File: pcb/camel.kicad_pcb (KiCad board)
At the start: 2 copper layers, 75 x 14 mm, 49 parts, among them J1 Conn_01x04, J2 Conn_01x04, Q1 MMBT4403, Q2 MMBT4403, U1 HX711, U2 HX711, U3 MCP1700T-3302E/TT, Y1 11.0592MHz, Y2 11.0592MHz

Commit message: first pass
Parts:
- removed the C13 at (159.3, 103.2)
- removed FPC1: FPC-05F-12PH15, EasyEDA2KiCAD:FPC-SMD_12P-P0.50_XUNPU_FPC-05F-12PH15
- removed JP1, JP4, JP6: SolderJumper_2_Bridged, Jumper:SolderJumper-2_P1.3mm_Bridged_RoundedPad1.0x1.5mm
- removed JP2, JP3: SolderJumper_3_Bridged12, Jumper:SolderJumper-3_P1.3mm_Bridged12_RoundedPad1.0x1.5mm
- removed JP5, JP7: SolderJumper_2_Open, Jumper:SolderJumper-2_P1.3mm_Open_RoundedPad1.0x1.5mm
- removed the R10 at (159.3, 101.8)
- removed the R9 at (138.2, 108.2)
- removed Y1, Y2: 11.0592MHz, Crystal:Crystal_SMD_5032-4Pin_5.0x3.2mm
- added C15: 100n, Capacitor_SMD:C_0402_1005Metric, F.Cu at (143.5, 103.8)
- added C3: 10n, Capacitor_SMD:C_0402_1005Metric, F.Cu at (157.3, 112.4)
- added C4: 1u, Capacitor_SMD:C_0402_1005Metric, F.Cu at (157.3, 113.5)
- added C7: 100n, Capacitor_SMD:C_0402_1005Metric, F.Cu at (138.4, 101.5)
- added C8: 100n, Capacitor_SMD:C_0402_1005Metric, F.Cu at (153.0, 105.1)
- added D1: RED, LED_SMD:LED_0603_1608Metric, F.Cu at (140.2, 94.7)
- added D10: RCLAMP0521P-N, camel:X1-DFN1006-2_L1.0-W0.6-BI, F.Cu at (144.3, 109.9)
- added D11: RCLAMP0521P-N, camel:X1-DFN1006-2_L1.0-W0.6-BI, F.Cu at (148.0, 109.9)
- added D2: RCLAMP0521P-N, camel:X1-DFN1006-2_L1.0-W0.6-BI, F.Cu at (154.9, 97.0)
- added D3: RCLAMP0521P-N, camel:X1-DFN1006-2_L1.0-W0.6-BI, F.Cu at (160.3, 91.9)
- added D4: RCLAMP0521P-N, camel:X1-DFN1006-2_L1.0-W0.6-BI, F.Cu at (163.1, 91.9)
- added D5: RCLAMP0521P-N, camel:X1-DFN1006-2_L1.0-W0.6-BI, F.Cu at (162.9, 98.2)
- added D6: RCLAMP0521P-N, camel:X1-DFN1006-2_L1.0-W0.6-BI, F.Cu at (160.1, 98.2)
- added D7: RCLAMP0521P-N, camel:X1-DFN1006-2_L1.0-W0.6-BI, F.Cu at (148.5, 100.3)
- added D8: RCLAMP0521P-N, camel:X1-DFN1006-2_L1.0-W0.6-BI, F.Cu at (145.7, 100.3)
- added D9: RCLAMP0521P-N, camel:X1-DFN1006-2_L1.0-W0.6-BI, F.Cu at (150.9, 109.9)
- added G***: LOGO, camel:camel_logo_10, F.Cu at (164.3, 115.7)
- added G***: LOGO, camel:camel_logo_10, B.Cu at (147.1, 102.7)
- added H3: MountingHole, MountingHole:MountingHole_3.5mm, F.Cu at (174.0, 95.0)
- added H4: MountingHole, MountingHole:MountingHole_3.5mm, F.Cu at (123.0, 115.0)
- added J2: TC2030-NL, Connector:Tag-Connect_TC2030-IDC-NL_2x03_P1.27mm_Vertical, F.Cu at (162.2, 95.1)
- added J3: USART, Connector_JST:JST_PH_S4B-PH-K_1x04_P2.00mm_Horizontal, F.Cu at (151.5, 97.6)
- added J5: I2C STEMMA, Connector_JST:JST_PH_S4B-PH-K_1x04_P2.00mm_Horizontal, F.Cu at (145.5, 112.4)
- added L1: 39n, Inductor_SMD:L_1008_2520Metric, F.Cu at (156.7, 115.8)
- added R4: 2K2, Resistor_SMD:R_0402_1005Metric, F.Cu at (140.2, 97.7)
- added R8: 10K, Resistor_SMD:R_0402_1005Metric, F.Cu at (143.1, 101.9)
- added U3: STM32L010F4P6, Package_SO:TSSOP-20_4.4x6.5mm_P0.65mm, F.Cu at (148.6, 104.9)
- C10: value 10u -> 100n; footprint Capacitor_SMD:C_0603_1608Metric -> Capacitor_SMD:C_0402_1005Metric
- C9: renamed from C14; value 0.1u -> 100n
- J1: footprint dualScaleBoard_hx711:Pad_1x04_P2.54mm -> camel:Pad_1x04_P2.54mm
- J4: renamed from J2; footprint dualScaleBoard_hx711:Pad_1x04_P2.54mm -> camel:Pad_1x04_P2.54mm
- U2: renamed from U1; footprint EasyEDA2KiCAD:SOP-16_L10.0-W3.9-P1.27-LS6.0-BL -> Package_SO:SOP-16_3.9x9.9mm_P1.27mm
- U4: renamed from U2; footprint EasyEDA2KiCAD:SOP-16_L10.0-W3.9-P1.27-LS6.0-BL -> Package_SO:SOP-16_3.9x9.9mm_P1.27mm
- moved C5 19.9 mm to (139.6, 112.0)
- moved U1 17.2 mm to (139.7, 115.6), turned to 0 degrees
- moved FID1 14.7 mm to (169.0, 93.0)
- moved FID2 14.7 mm to (128.0, 93.0)
- moved FID3 14.7 mm to (128.0, 117.0)
- moved H1 12.8 mm to (123.0, 95.0)
- moved H2 12.8 mm to (174.0, 115.0)
- moved Q1 10.3 mm to (129.2, 97.8)
- moved Q2 10.1 mm to (168.1, 112.0)
- moved C2 9.74 mm to (132.0, 98.7), turned to 0 degrees
- moved C1 9.18 mm to (164.6, 111.0), turned to 180 degrees
- moved C6 8.83 mm to (136.5, 115.4), turned to 90 degrees
- moved C20 8.11 mm to (167.1, 102.8), turned to -90 degrees
- moved C14 7.33 mm to (129.3, 106.6), turned to 90 degrees
- moved R10 5.78 mm to (167.4, 105.2), turned to 90 degrees
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- renumbered C15 to C1, C1 to C11, C3 to C12, C5 to C13, C7 to C14, C2 to C17, C4 to C18, C6 to C19, C9 to C2, C8 to C20, C11 to C5, C12 to C6, H101 to H1, H102 to H2, L1 to L2, L2 to L3, R5 to R1, R8 to R10, R3 to R11, R4 to R12, R6 to R2, R1 to R3, R2 to R5, R7 to R9, U3 to U1
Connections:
- C1 pad 1: VCC -> +5VA
- C10 pad 1: VCC -> +3V3
- C2 pad 1: VCC -> +5VA
- C5 pad 1: VCC -> +5V
- C6 pad 1: VDD -> +3V3
- C9 pad 1: VDD -> +3V3
- Q1 pad 2: VCC -> +5VA
- Q2 pad 2: VCC -> +5VA
- U1 pad 2: /VO -> +3V3
- U1 pad 3: VCC -> +5V
- U2 pad 1: VCC -> +5VA
- U2 pad 13: Net-(U1-XO) -> unconnected-(U2-XO-Pad13)
- U2 pad 14: Net-(JP1-A) -> GND
- U2 pad 15: Net-(JP2-C) -> GND
- U2 pad 16: VDD -> +3V3
- U4 pad 1: VCC -> +5VA
- U4 pad 13: Net-(U2-XO) -> unconnected-(U4-XO-Pad13)
- U4 pad 14: Net-(JP4-A) -> GND
- U4 pad 15: Net-(JP3-C) -> GND
- U4 pad 16: VDD -> +3V3
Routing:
- net +3V3: track 0.00 -> 120.2 mm, vias 0 -> 7
- net GND: track 12.3 -> 109.3 mm, vias 44 -> 99
- net +5VA: track 0.00 -> 66.5 mm, vias 0 -> 2
- net VDD: track 51.7 -> 0.00 mm, vias 4 -> 0
- net VCC: track 47.4 -> 0.00 mm, vias 4 -> 0
- net /I2C_SDA: track 0.00 -> 28.1 mm, vias 0 -> 2
- net /I2C_SCL: track 0.00 -> 25.4 mm, vias 0 -> 1
- net +5V: track 0.00 -> 24.8 mm
- net /NRST: track 0.00 -> 23.2 mm, vias 0 -> 2
- net /SWDIO: track 0.00 -> 18.1 mm
- net /SWCLK: track 0.00 -> 17.6 mm, vias 0 -> 2
- net /SCK2: track 25.8 -> 10.4 mm
- net /USART_TX: track 0.00 -> 12.3 mm
- net /USART_RX: track 0.00 -> 12.3 mm
- net Net-(Q1-C): track 17.6 -> 29.3 mm
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- added copper zone on In1.Cu, net GND
- added copper zone on In2.Cu, net GND
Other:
- board size 75 x 14 mm -> 59 x 28 mm
- copper layers 2 -> 4
- board text added: "3V3"
- board text added: "5V"
- board text added: "GND"
- board text added: "I2C"
- board text added: "L"
- board text added: "R"
- board text added: "RX"
- board text added: "Rev 1.0"
- board text added: "SCL"
- board text added: "SDA"
- board text added: "SWD"
- board text added: "TX"
- board text added: "USART"
- board text removed: "DSBHX711 Rev 1.0"

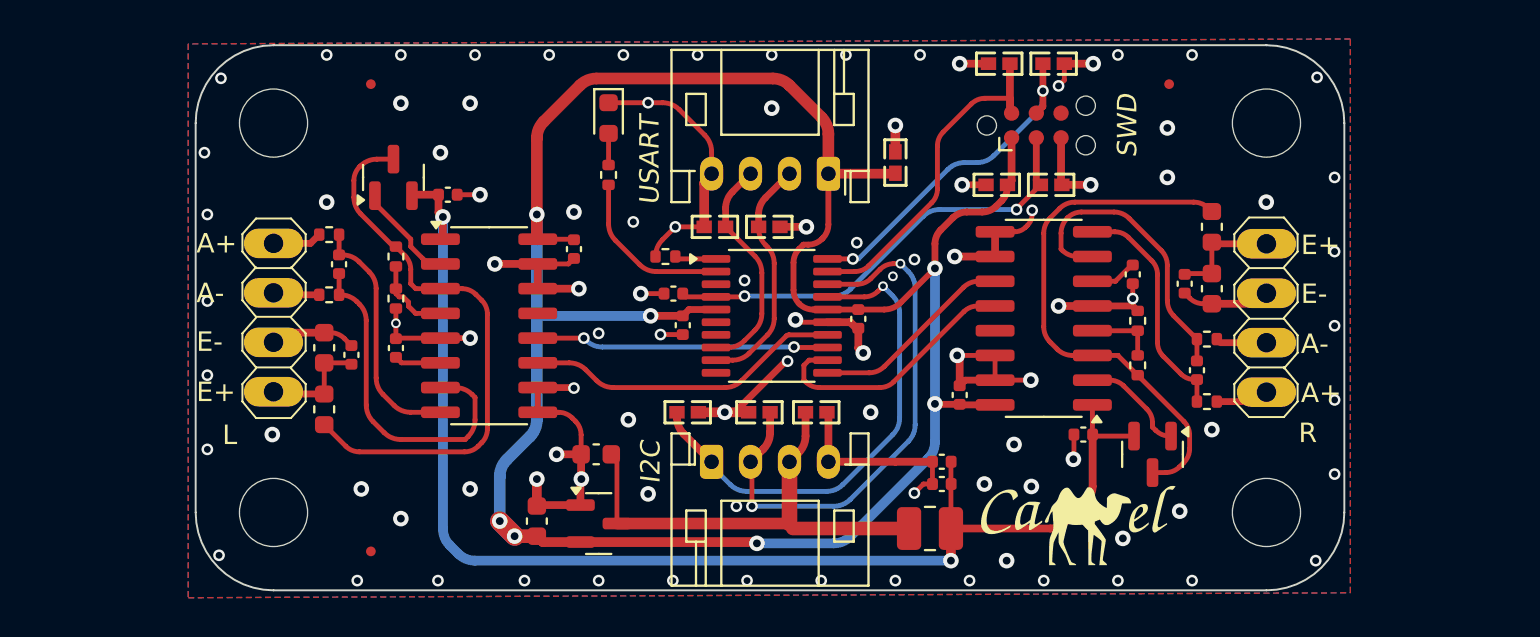
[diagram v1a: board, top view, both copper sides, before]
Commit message: added extra SWD connector in addition to TagConnect
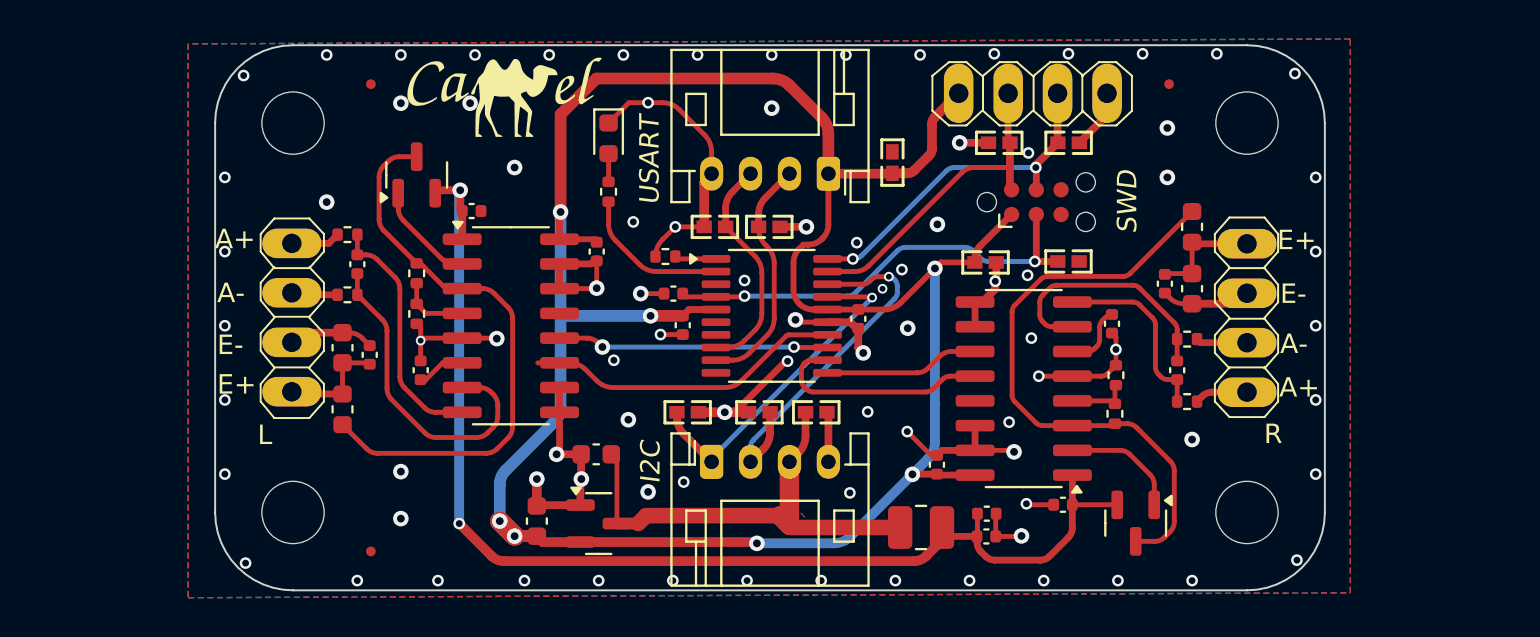
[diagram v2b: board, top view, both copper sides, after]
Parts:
- added J6: Conn_01x04, camel:Pad_1x04_P2.54mm, F.Cu at (158.2, 93.5)
- H1, H2, H3, H4: footprint MountingHole:MountingHole_3.5mm -> MountingHole:MountingHole_3.2mm_M3
- moved G*** 36.8 mm to (134.9, 93.7)
- moved D4 4.14 mm to (163.8, 96.0)
- moved D3 4.06 mm to (160.3, 96.0)
- moved D5 4.04 mm to (163.8, 102.1)
- moved D6 4.03 mm to (159.6, 102.2), turned to 0 degrees
- moved J2 3.94 mm to (162.2, 99.1)
- moved C9 3.77 mm to (157.1, 112.5)
- moved C1 3.75 mm to (163.5, 114.6)
- moved U4 3.75 mm to (161.5, 108.6)
- moved Q2 3.64 mm to (167.3, 115.5)
- moved C4 3.53 mm to (159.6, 116.2), turned to 0 degrees
- moved C3 3.53 mm to (159.6, 115.1), turned to 0 degrees
- moved R10 3.01 mm to (166.3, 108.0)
- moved C20 2.75 mm to (166.1, 105.3)
- moved R9 2.75 mm to (166.2, 109.9)
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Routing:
- net GND: track 109.3 -> 90.7 mm, vias 99 -> 89
- net /I2C_SDA: track 28.1 -> 19.0 mm, vias 2 -> 1
- net /I2C_SCL: track 25.4 -> 17.4 mm
- net +5VA: track 66.5 -> 62.1 mm
- net Net-(Q2-C): track 27.8 -> 31.0 mm
- net Net-(U4-INA-): track 15.4 -> 12.8 mm
- net /SCK2: track 10.4 -> 7.96 mm
- net Net-(U4-INA+): track 12.0 -> 9.58 mm
- net Net-(J4-Pin_3): track 2.62 -> 5.00 mm
- net /DOUT2: track 13.7 -> 11.7 mm
- net /SWDIO: track 18.1 -> 16.5 mm
- net /DOUT1: track 15.0 -> 13.9 mm
- net +3V3: track 120.2 -> 121.3 mm
- net Net-(U2-INA-): track 17.8 -> 16.8 mm
- net Net-(U4-VBG): track 2.42 -> 3.36 mm
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- added copper zone on F.Cu, net +5V
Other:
- board size 59 x 28 mm -> 57 x 28 mm
- board text added: "CLK"
- board text added: "DIO"

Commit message: replaced with hx712, updated schematics and pcb
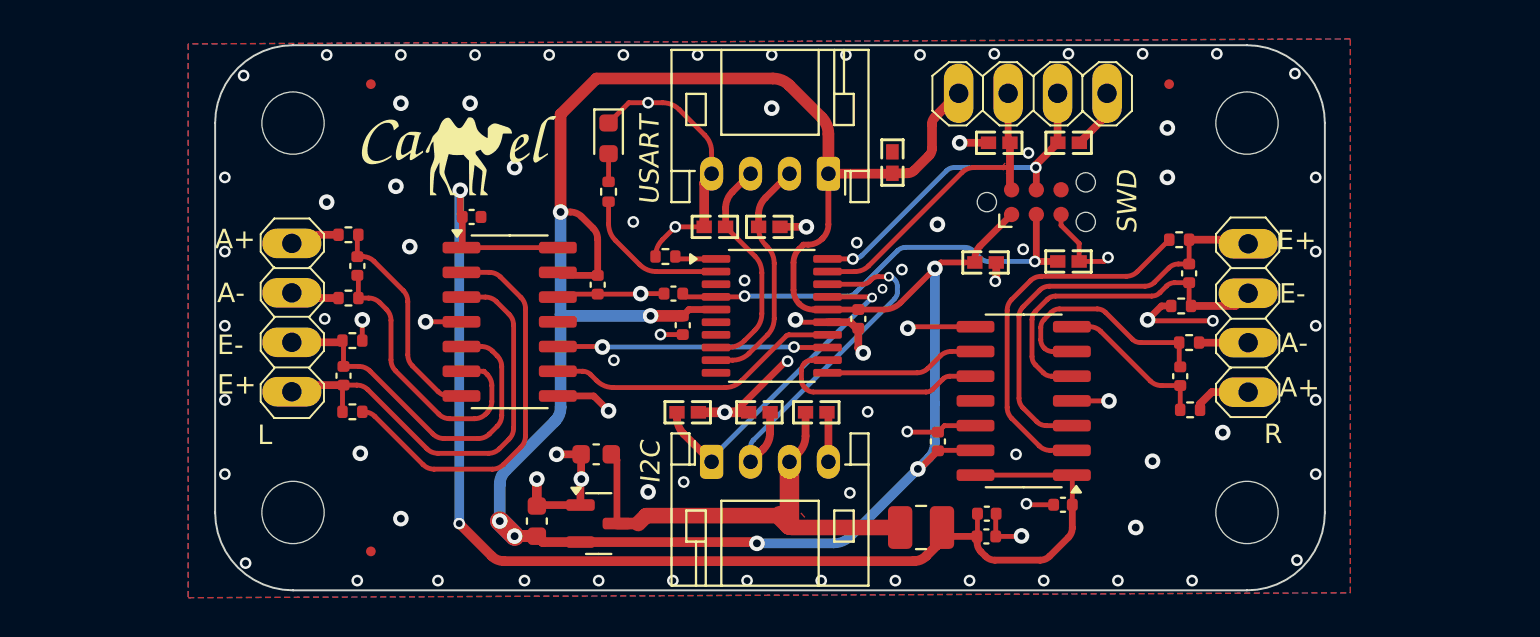
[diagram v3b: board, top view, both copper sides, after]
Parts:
- removed the C12 at (126.5, 106.5)
- removed C17, C19, C20: 0.1u, Capacitor_SMD:C_0402_1005Metric
- removed C18: 10u, Capacitor_SMD:C_0603_1608Metric
- removed the J4 at (173.0, 101.2)
- removed L2, L3: 3.3u, Inductor_SMD:L_0603_1608Metric
- removed Q1, Q2: MMBT4403, Package_TO_SOT_SMD:SOT-23
- removed R11, R12: 100R, Resistor_SMD:R_0402_1005Metric
- removed the R5 at (126.8, 103.8)
- added C15: 0.1u, Capacitor_SMD:C_0402_1005Metric, F.Cu at (169.6, 108.0)
- added J5: Conn_01x04, camel:Pad_1x04_P2.54mm, F.Cu at (173.1, 101.2)
- added R4: 200R, Resistor_SMD:R_0402_1005Metric, F.Cu at (126.8, 100.7)
- added R7: 100R, Resistor_SMD:R_0402_1005Metric, F.Cu at (169.5, 101.0)
- added R8: 100R, Resistor_SMD:R_0402_1005Metric, F.Cu at (169.6, 104.4)
- R1: value 20K -> 100R
- R10: value 8K2 -> 200R
- R2: value 8K2 -> 100R
- R3: value 100R -> 200R
- R9: value 20K -> 200R
- U2, U4: value HX711 -> HX712; footprint Package_SO:SOP-16_3.9x9.9mm_P1.27mm -> Package_SO:SOIC-14_3.9x8.7mm_P1.27mm
- moved C14 39.8 mm to (170.0, 102.7), turned to -90 degrees
- moved R1 7.84 mm to (127.1, 109.8), turned to 0 degrees
- moved R9 5.28 mm to (170.0, 106.3), turned to 180 degrees
- moved R10 4.20 mm to (170.1, 109.7), turned to 180 degrees
- moved G*** 3.80 mm to (132.5, 96.7)
- moved R2 3.58 mm to (127.0, 106.2), turned to 180 degrees
- moved R3 3.26 mm to (126.8, 104.0)
- moved C11 1.72 mm to (126.6, 108.0)
- moved C7 1.71 mm to (139.6, 103.3)
- moved C9 1.20 mm to (157.1, 111.4)
- moved U4 0.64 mm to (161.5, 109.3)
- moved C2 0.30 mm to (133.2, 99.8)
- moved U2 0.21 mm to (135.1, 105.2)
- moved C12 0.09 mm to (127.3, 102.3), turned to 90 degrees
- renumbered C13 to C12, C15 to C13, D2 to D1, D9 to D11, D5 to D2, D4 to D3, D3 to D4, D1 to D5, D11 to D9, J6 to J2, J2 to J3, J3 to J4, J5 to J6, R4 to R5, R8 to R6
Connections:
- C11 pad 2: GND -> Net-(J1-Pin_2)
- C12 pad 1: Net-(U2-INA+) -> Net-(U2-INN)
- C14 pad 1: Net-(U2-VBG) -> Net-(J5-Pin_1)
- C14 pad 2: GND -> Net-(J5-Pin_2)
- J1 pad 2: GND -> Net-(J1-Pin_2)
- R1 pad 1: Net-(Q1-C) -> Net-(J1-Pin_1)
- R1 pad 2: Net-(U2-VFB) -> Net-(U2-VOUT)
- R10 pad 1: Net-(U4-VFB) -> Net-(J5-Pin_4)
- R10 pad 2: GND -> Net-(U4-INP)
- R2 pad 1: Net-(U2-VFB) -> GND
- R2 pad 2: GND -> Net-(J1-Pin_2)
- R3 pad 1: Net-(J1-Pin_4) -> Net-(J1-Pin_3)
- R3 pad 2: Net-(U2-INA+) -> Net-(U2-INN)
- R9 pad 1: Net-(Q2-C) -> Net-(J5-Pin_3)
- R9 pad 2: Net-(U4-VFB) -> Net-(U4-INN)
- U2 pad 10: GND -> /DOUT1
- U2 pad 11: /SCK1 -> unconnected-(U2-XO-Pad11)
- U2 pad 12: /DOUT1 -> GND
- U2 pad 13: unconnected-(U2-XO-Pad13) -> +3V3
- U2 pad 14: GND -> +5VA
- U2 pad 2: Net-(Q1-B) -> Net-(U2-VOUT)
- U2 pad 3: Net-(Q1-C) -> Net-(J1-Pin_1)
- U2 pad 4: Net-(U2-VFB) -> GND
- U2 pad 5: GND -> Net-(J1-Pin_2)
- U2 pad 6: Net-(U2-VBG) -> Net-(U2-INN)
- U2 pad 8: Net-(U2-INA+) -> GND
- U2 pad 9: GND -> /SCK1
- U4 pad 10: GND -> /DOUT2
- U4 pad 11: /SCK2 -> unconnected-(U4-XO-Pad11)
- U4 pad 12: /DOUT2 -> GND
- U4 pad 13: unconnected-(U4-XO-Pad13) -> +3V3
- U4 pad 14: GND -> +5VA
- U4 pad 3: Net-(Q2-C) -> Net-(J5-Pin_1)
- U4 pad 4: Net-(U4-VFB) -> GND
- U4 pad 5: GND -> Net-(J5-Pin_2)
- U4 pad 6: Net-(U4-VBG) -> Net-(U4-INN)
- U4 pad 7: Net-(U4-INA-) -> Net-(U4-INP)
- U4 pad 8: Net-(U4-INA+) -> GND
- U4 pad 9: GND -> /SCK2
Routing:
- net Net-(Q2-C): track 31.0 -> 0.00 mm
- net Net-(Q1-C): track 29.5 -> 0.00 mm
- net Net-(J5-Pin_1): track 0.00 -> 21.9 mm
- net Net-(U2-VOUT): track 0.00 -> 21.1 mm
- net Net-(J1-Pin_2): track 0.00 -> 19.3 mm
- net Net-(J1-Pin_1): track 5.68 -> 23.6 mm
- net Net-(J5-Pin_2): track 0.00 -> 17.8 mm
- net Net-(U2-INN): track 0.00 -> 15.4 mm
- net Net-(U4-VOUT): track 6.08 -> 19.2 mm
- net Net-(U4-INA-): track 12.8 -> 0.00 mm
- net GND: track 90.7 -> 78.0 mm, vias 89 -> 93
- net Net-(U2-INA+): track 12.7 -> 0.00 mm
- net Net-(U4-INN): track 0.00 -> 12.1 mm
- net Net-(U4-INA+): track 9.58 -> 0.00 mm
- net Net-(U4-INP): track 0.00 -> 7.99 mm
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- added copper zone on F.Cu, net /SWDIO

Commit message: PCB updates, teardrops and trace cleanup
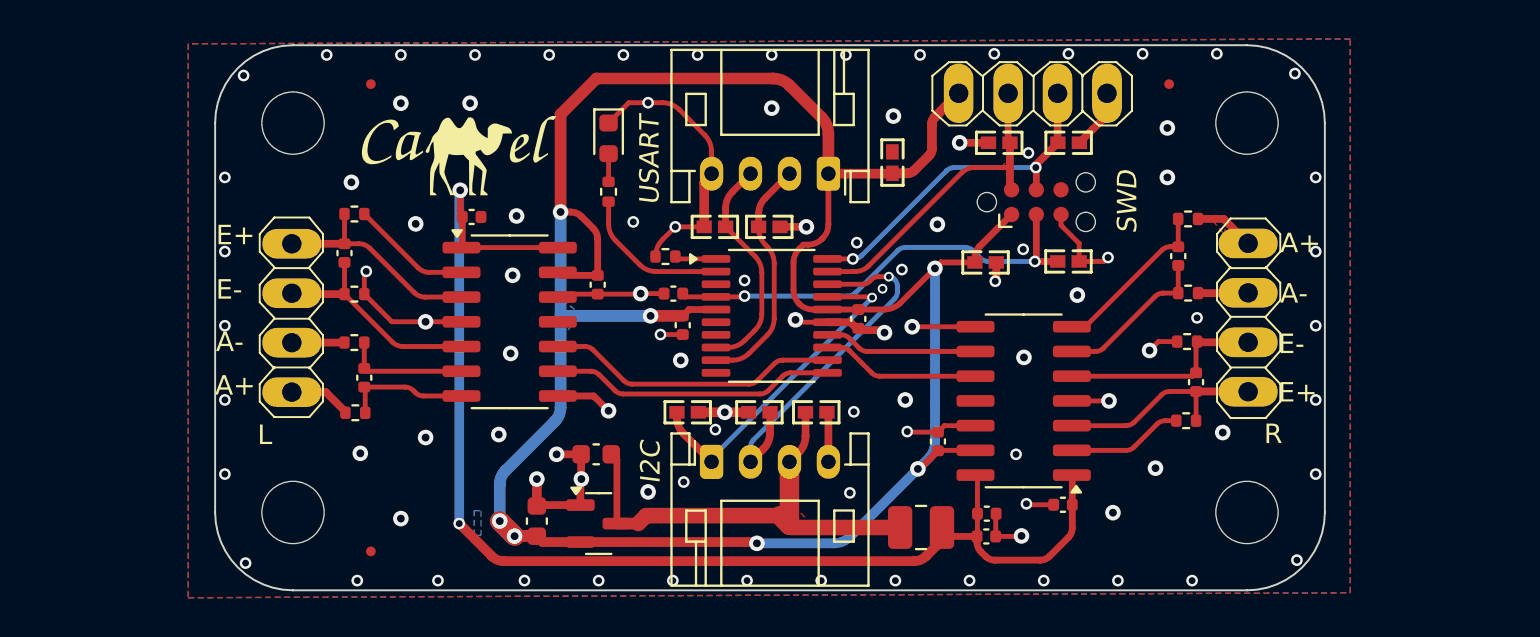
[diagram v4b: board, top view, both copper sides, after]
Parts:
- removed the G*** at (147.1, 102.7)
- added G***: LOGO, camel:camel_logo_30, B.Cu at (148.1, 105.3)
- moved R1 10.2 mm to (127.2, 99.7)
- moved R10 9.80 mm to (170.0, 99.9)
- moved R7 9.30 mm to (169.9, 110.3)
- moved R4 9.15 mm to (127.2, 109.9)
- moved J1 7.60 mm to (123.9, 101.2), turned to 0 degrees
- moved J5 7.60 mm to (173.1, 108.8), turned to 180 degrees
- moved C11 6.30 mm to (126.6, 101.7), turned to -90 degrees
- moved C15 6.17 mm to (169.5, 101.8), turned to 90 degrees
- moved C12 5.75 mm to (127.7, 108.1), turned to -90 degrees
- moved C14 5.60 mm to (170.4, 108.3), turned to 90 degrees
- moved R9 2.54 mm to (170.0, 103.7)
- moved R2 2.39 mm to (127.2, 103.8)
- moved R3 2.31 mm to (127.2, 106.3)
- moved R8 1.85 mm to (169.9, 106.2)
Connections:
- net +5V renamed VDD
- net +5VA renamed VDDA
- net Net-(J1-Pin_1) renamed /L_REFP
- net Net-(J1-Pin_2) renamed /L_REFN
- net Net-(J5-Pin_1) renamed /R_REFP
- net Net-(J5-Pin_2) renamed /R_REFN
- net Net-(U2-INN) renamed /L_INN
- net Net-(U2-INP) renamed /L_INP
- net Net-(U2-VOUT) renamed /L_VOUT
- net Net-(U4-INN) renamed /R_INN
- net Net-(U4-INP) renamed /R_INP
- net Net-(U4-VOUT) renamed /R_VOUT
- U3 pad 11: /SCK2 -> /SCK1
- U3 pad 12: /DOUT2 -> /DOUT1
- U3 pad 13: /DOUT1 -> /DOUT2
- U3 pad 14: /SCK1 -> /SCK2
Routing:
- net /L_VOUT: track 21.1 -> 6.19 mm
- net /R_VOUT: track 19.2 -> 5.93 mm
- net /L_REFP: track 23.6 -> 11.3 mm
- net /R_REFP: track 21.9 -> 11.2 mm
- net /L_INN: track 15.4 -> 6.38 mm
- net /L_REFN: track 19.3 -> 11.4 mm
- net /R_REFN: track 17.8 -> 10.7 mm
- net /L_INP: track 11.3 -> 6.47 mm
- net /R_INN: track 12.1 -> 8.07 mm
- net /DOUT2: track 11.7 -> 8.16 mm
- net GND: track 78.0 -> 74.6 mm, vias 93 -> 99
- net VDDA: track 68.8 -> 65.9 mm
- net /DOUT1: track 13.9 -> 15.0 mm, vias 2 -> 0
- net Net-(J1-Pin_4): track 2.58 -> 3.22 mm
- net /R_INP: track 7.99 -> 8.54 mm
- added copper zone on B.Cu, net +3V3
- added copper zone on F.Cu, net Net-(J5-Pin_4)
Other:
- board text added: "Rev 2.0"
- board text added: "VCC"
- board text removed: "5V"
- board text removed: "Rev 1.0"
